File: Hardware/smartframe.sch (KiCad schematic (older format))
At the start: 40 parts, among them J1 USB_B, J2 Micro_SD_Card, SW1 Reset, U1 F1C100s, U3 JW5211, U4 JW5211, U5 JW5211, Y1 24MHz

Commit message: Creating MIC23450 footprint, updating schematic
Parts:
- removed C20: 100n, symbol Device:C
- removed C3, C4: 2.2u, symbol Device:C
- removed C5, C7, C8: 22u, symbol Device:C
- removed L1, L2, L3: 2.2u, symbol Device:L
- removed R1: 49.9k, symbol Device:R
- removed R2, R4: 11k, symbol Device:R
- removed R3: 36k, symbol Device:R
- removed R5: 8.2k, symbol Device:R
- removed R6: 10k, symbol Device:R
- removed U3, U4, U5: JW5211, Package_TO_SOT_SMD:SOT-23-5, symbol 3340-assorted:JW5211
- added C20: 100n, symbol Device:C_Small
- added R10, R11, R12, R13, R9: 49.9k, symbol Device:R
- added U?: MIC23450, symbol MIC23450:MIC23450
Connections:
- wire segments 60 -> 67
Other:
- moved on the sheet: C10, C11, C12, C13, C14, C15, C16, C17, C18, C19, C9, F1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

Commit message: Updating power delivery
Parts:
- added C21, C23, C24, C25: 4.7u, symbol Device:C
- added C22: 100n, symbol Device:C
- added L1, L2, L3: 1u, symbol Device:L
- added R14: 50, symbol Device:R
- added R15, R17, R19: 137k, symbol Device:R_Small
- added R16: 174k, symbol Device:R_Small
- added R18: 43.2k, symbol Device:R_Small
- added R20: 31.6k, symbol Device:R_Small
- gave numbers to parts that had none: 1
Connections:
- net 1.1V: now also U2.31 (SNS1), C23.1, L1.2, R15.1
- net 2.6V: now also U2.4 (SNS2), C24.1, L2.2, R17.1
- net 3.3V: now also U2.9 (SNS3), C25.1, L3.2, R19.1
- net FUSE_PWR: now also U2.14 (PVIN3), U2.27 (PVIN1), U2.29 (PVIN2), U2.3 (EN2), U2.30 (EN1), U2.8 (EN3), C21.1, R14.1
- net GND: now also U2.11 (AGND3), U2.18 (PGND3), U2.2 (AGND1), U2.22 (PGND2), U2.24 (PGND1), U2.7 (AGND2), C21.2, C22.2, C23.2, C24.2, C25.2, R16.2, R18.2, R20.2
- net at U2.10 (FB3): now also R19.2, R20.1
- net at U2.13 (AVIN3): now also U2.15 (AVIN2), U2.28 (AVIN1), C22.1, R14.2
- net at U2.21 (SW3): now also L3.1
- net at U2.23 (SW2): now also L2.1
- net at U2.26 (SW1): now also L1.1
- net at U2.32 (FB1): now also R15.2, R16.1
- net at U2.5 (FB2): now also R17.2, R18.1
- no-connect marks 50 -> 53
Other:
- moved on the sheet: C1, C10, C11, C12, C13, C14, C15, C16, C17, C18, C19, C2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

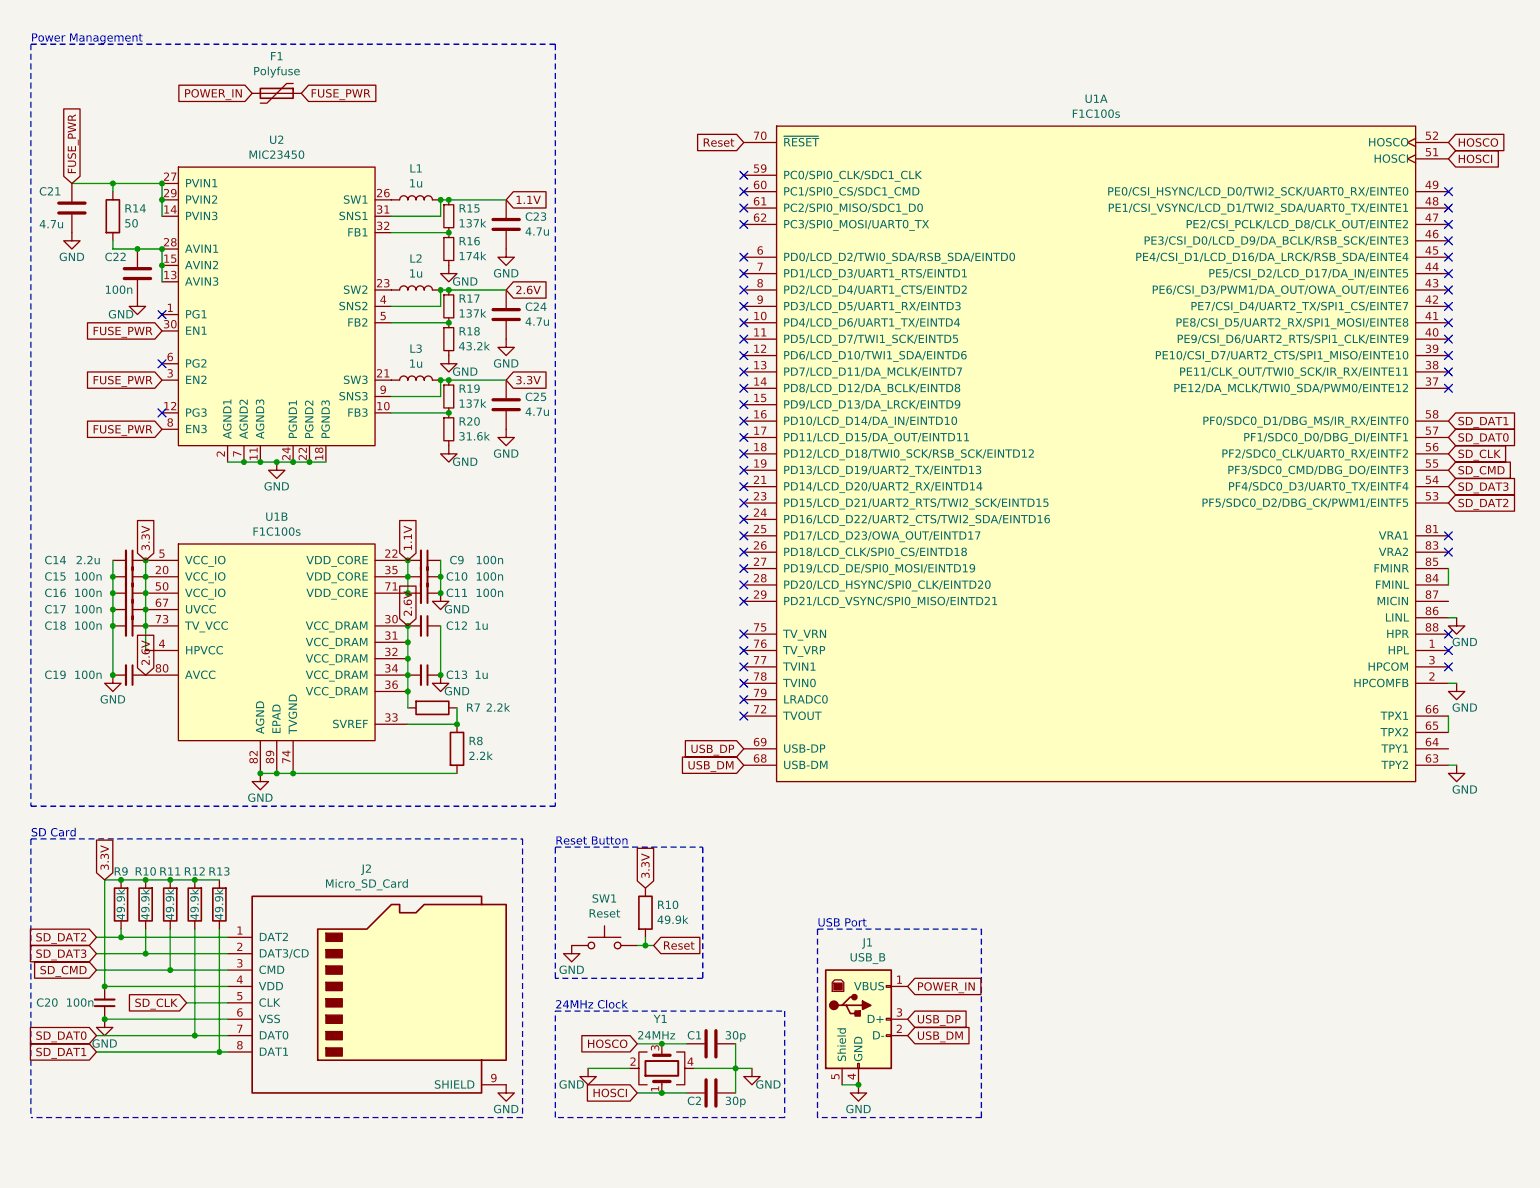
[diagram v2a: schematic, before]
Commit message: Adding more logical annotations
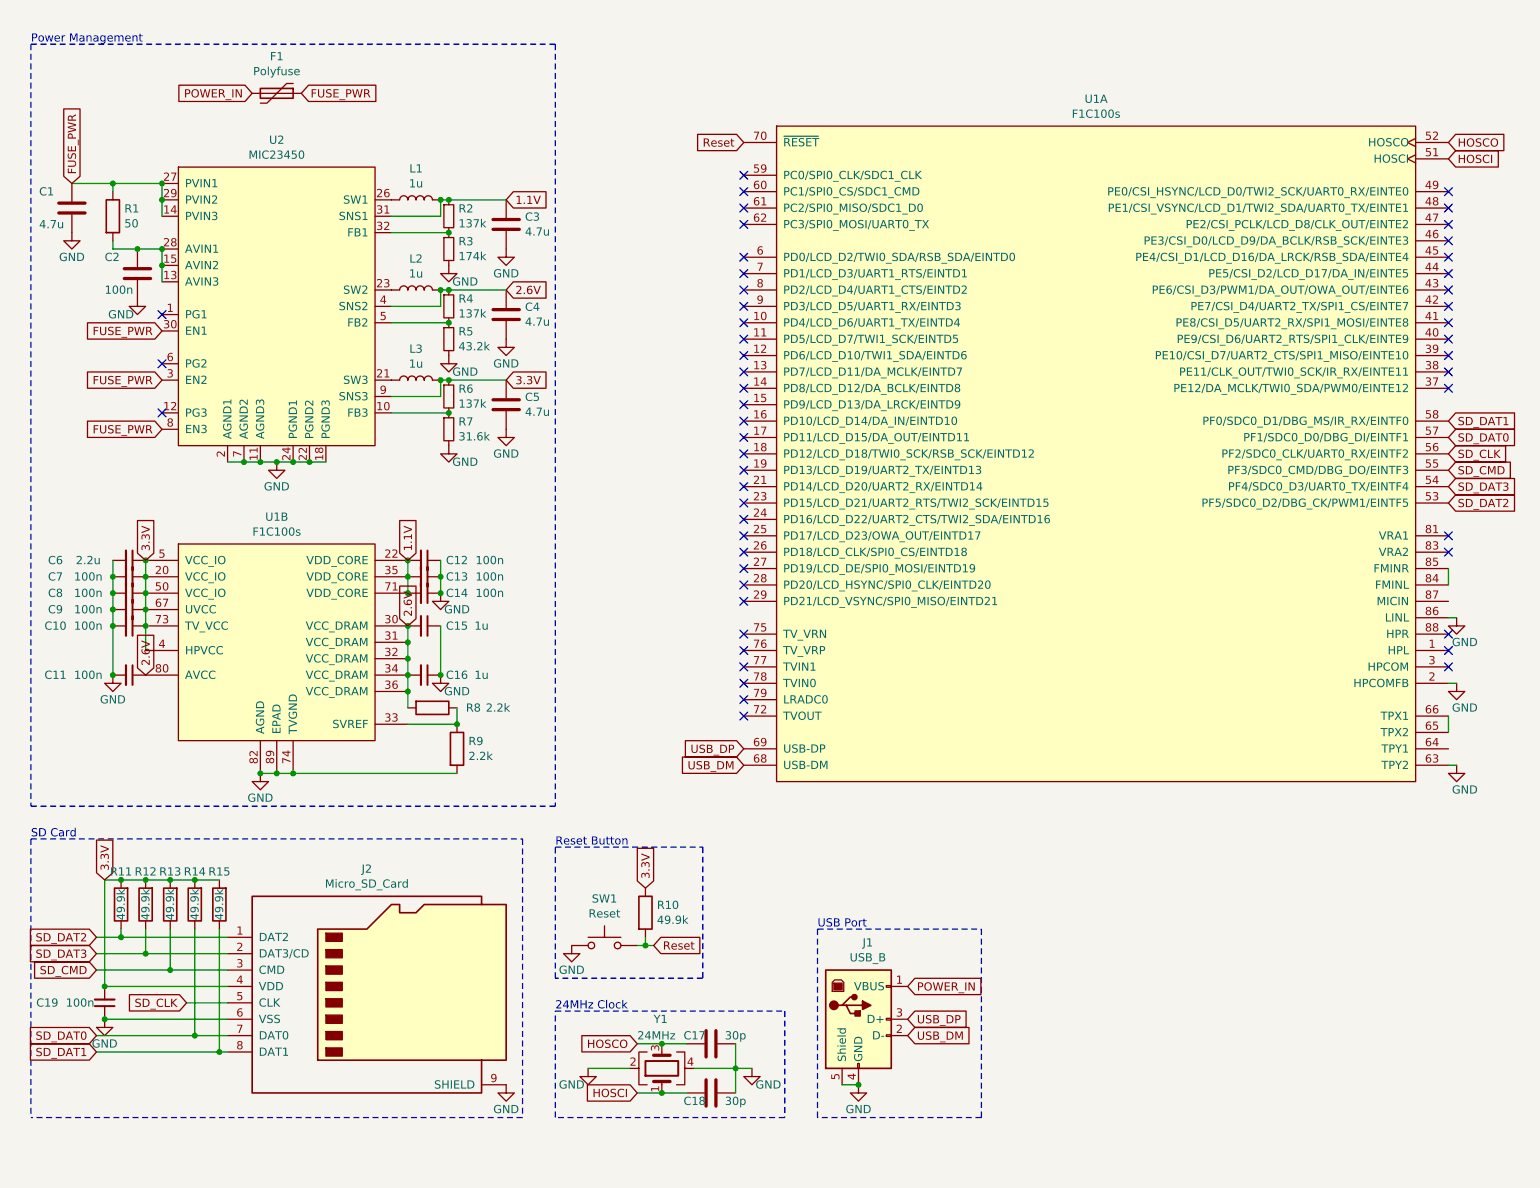
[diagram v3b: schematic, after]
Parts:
- renumbered C21 to C1, C18 to C10, C19 to C11, C9 to C12, C10 to C13, C11 to C14, C12 to C15, C13 to C16, C1 to C17, C2 to C18, C20 to C19, C22 to C2, C23 to C3, C24 to C4, C25 to C5, C14 to C6, C15 to C7, C16 to C8, C17 to C9, R14 to R1, R9 to R11, R10 to R12, R11 to R13, R12 to R14, R13 to R15, R15 to R2, R16 to R3, R17 to R4, R18 to R5, R19 to R6, R20 to R7, R7 to R8, R8 to R9
